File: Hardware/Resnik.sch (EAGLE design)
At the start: 194 parts, among them IC1 ATMEGA644M, J1 CONN_82.54_SCREW, J3 CONN_42.54_SCREW, J4 CONN_82.54_SCREW, Q1 DMG3404, Q2 DMG3404, Q3 FDN360P, Q4 FDN360P, Q5 FDN360P, Q6 DMG3404, U1 TLV61220DBV, U10 TPS22917DBV, U11 SN74AUP1G04YFP, U12 SN74AUP1G04YFP, U13 SN74AUP2G86SOT833-1, U14 SN74AUP2G08DQE, U15 SN74AUP2G08DQE, U16 SN74AUP2G08DQE, U17 MIC2544MSOP, U18 MIC2544MSOP, U19 MIC2544MSOP, U2 TPS62822DLC, U20 MIC2544MSOP, U21 TPS22917DBV, U22 TPS22917DBV, U23 FT231X-Q, U24 SN74LVC1G3157DRL, U25 SN74AUP3G34DCU, U26 TXS0102DQM, U27 TXS0108RGY, U28 TXS0108RGY, U29 TXS0104RGY, U3 TPS61032RSA, U30 MCP4726A2SOT-23, U31 BME280, U32 ADS1115, U33 ADS1115, U34 INA211DCK, U35 INA210DCK, U36 TCA9535RTW, U37 TLV3691DCK, U38 TS5A21366RSE, U39 MIC94090C6, U5 BQ2980RUG, U6 TPS2105, U7 LTC4412S6, U8 TPL5111DDC, U9 TPS79733

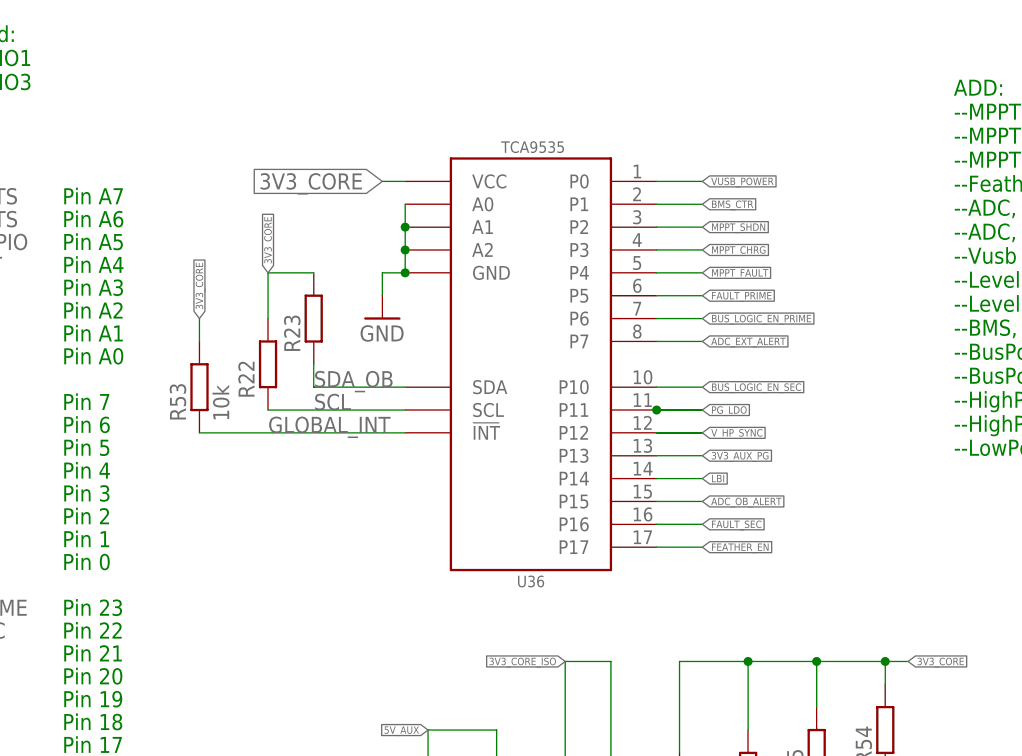
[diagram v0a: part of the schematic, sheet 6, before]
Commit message: Initial updates for v0.3
Additional routing required, need to add ADC switch enable, need to add efficiency modification to mppt
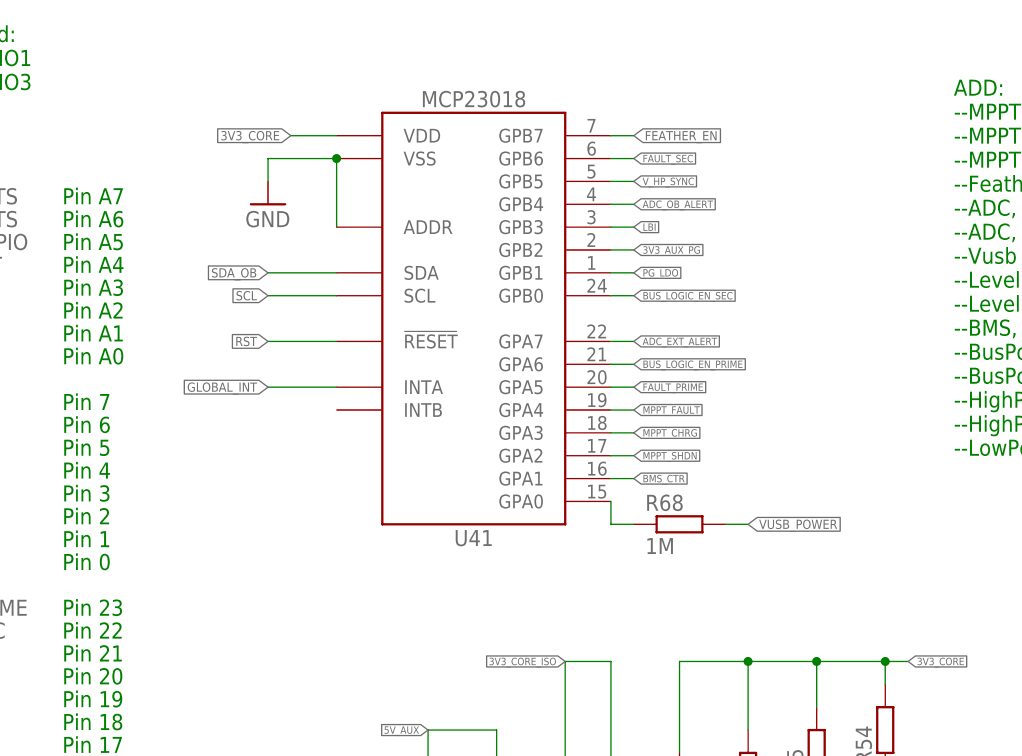
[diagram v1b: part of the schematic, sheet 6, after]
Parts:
- removed R22: (no value), bschulz_passives:R-EU_R0402
- removed U36: TCA9535RTW, bschulz:TCA9535RTW
- added Q7: 2N7002, bschulz:MOSFET-NCH-2N7002PW
- added R63: 100k, bschulz_passives:R-EU_100KR0402
- added R64, R68: 1M, bschulz_passives:R-EU_1MR0402
- added R65, R66: 180k, bschulz_passives:R-EU_180KR0402
- added R67: 10k, bschulz_passives:R-EU_10KR0402
- added U40: SN74AHC1G86DCK, bschulz:SN74AHC1G86DCK
- added U41: MCP23018QFN, bschulz:MCP23018QFN
- R23: value (none) -> 100k; device bschulz_passives:R-EU_R0402 -> bschulz_passives:R-EU_100KR0402
- R53: value 10k -> 1M; device bschulz_passives:R-EU_10KR0402 -> bschulz_passives:R-EU_1MR0402
- U13: value SN74AUP2G86SOT833-1 -> SN74AUP1G04YFP; device bschulz:SN74AUP2G86SOT833-1 -> bschulz:SN74AUP1G04YFP
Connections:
- removed net N$22: U13.Y1, U16.A1
- removed net N$25: U13.Y2, U16.A2
- new net N$17: R68.1, U41.GPA0
- new net N$68: Q7.G, U13.Y
- new net POWER_EN: U13.A, U16.A1, U16.A2, U2.EN, U3.EN, U40.Y
- new net VCC: U40.VCC
- net 3V3_AUX_PG: now also U41.GPB2; no longer U36.P13
- net 3V3_CORE: now also U41.VDD; no longer R22.2, R23.2, R53.2, U36.VCC
- net 3V3_CORE_ISO: now also R23.2
- net 5V_AUX: now also Q7.D, R67.2; no longer U2.EN
- net ADC_EXT_ALERT: now also U41.GPA7; no longer U36.P7
- net ADC_OB_ALERT: now also U41.GPB4; no longer U36.P15
- net BMS_CTR: now also U41.GPA1; no longer U36.P1
- net BUS_LOGIC_EN_PRIME: now also U41.GPA6; no longer U36.P6
- net BUS_LOGIC_EN_SEC: now also U41.GPB0; no longer U36.P10
- net C0: now also U40.A, U40.B; no longer U13.A1, U13.B2
- net C1: no longer U13.A2, U13.B1
- net FAULT_PRIME: now also U41.GPA5; no longer U36.P5
- net FAULT_SEC: now also U41.GPB6; no longer U36.P16
- net FEATHER_EN: now also U41.GPB7; no longer U36.P17
- net GLOBAL_INT: now also U41.INTA; no longer R53.1, U36.!INT
- net GND: now also Q7.S, R23.1, R53.1, R63.1, R64.1, R65.1, R66.1, R67.1, U40.GND, U41.ADDR, U41.VSS; no longer U36.A0, U36.A1, U36.A2, U36.GND
- net LBI: now also U41.GPB3; no longer U36.P14
- net MPPT_CHRG: now also U41.GPA3; no longer U36.P3
- net MPPT_FAULT: now also U41.GPA4; no longer U36.P4
- net MPPT_SHDN: now also U41.GPA2; no longer U36.P2
- net PG_LDO: now also U41.GPB1; no longer U36.P11
- net RST: now also U41.!RESET
- net SCL: now also U41.SCL; no longer R22.1, U36.SCL
- net SDA_OB: now also U41.SDA; no longer R23.1, U36.SDA
- net VBUS_PRIME: now also R65.2
- net VBUS_SEC: now also R66.2
- net VUSB_POWER: now also R63.2, R68.2; no longer U36.P0
- net V_HP: no longer U3.EN
- net V_HP_SYNC: now also U41.GPB5; no longer U36.P12
- net V_LI_SENSE: now also R64.2
- net V_PRIME_SENSE: now also R53.2
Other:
- moved on the sheet: C1, R1, R2, R3, R8

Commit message: Layout updates, cleanup required, minor testing
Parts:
- removed R54: (no value), bschulz_passives:R-EU_R0402
- added Q8: 2N7002, bschulz:MOSFET-NCH-2N7002PW
- added R22, R69, R70, R71: (no value), bschulz_passives:R-EU_R0603
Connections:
- removed net N$67: C10.1, D1.C, U4.VIN, U4.VIN_REG
- removed net VCC: U40.VCC
- new net ADC_SENSE_SW: IC1.(PCINT8/XCK0/T0)PB0, U38.S1, U38.S2
- new net MPPT_VIN_REG: R22.1, R69.2, U4.VIN_REG
- new net N$22: Q8.D, R70.1
- new net V_SOLAR_IN: C10.1, D1.C, R22.2, R71.2, U4.VIN
- net 3V3_CORE: now also U40.VCC; no longer R54.2
- net 5V_AUX: no longer U38.S1, U38.S2
- net C0: no longer U40.B
- net C1: now also U40.B
- net GND: now also Q8.S, R69.1
- net MPPT_CHRG: now also Q8.G
- net MPPT_SHDN: now also R70.2, R71.1; no longer R54.1, U41.GPA2

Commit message: Continued layout, generated gerbers
Improved layout, generated gerbers, final design review before send to fab
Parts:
- added D8: BAT54C, bschulz:BAT54C
- R18: value 5m -> 50m; device bschulz_passives:R-EU_0.005R0805 -> bschulz_passives:R-EU_0.05R0805
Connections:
- new net N$69: D8.C, U37.VCC
- net 5V_LP: now also D8.A2
- net V_CORE: no longer U37.VCC
- net V_PRIME: now also D8.A1
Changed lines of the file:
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@@
 <setting verticaltext="up"/>
 </settings>
-<grid distance="0.1" unitdist="inch" unit="mm" style="lines" multiple="1" display="no" altdistance="0.01" altunitdist="inch" altunit="mm"/>
+<grid distance="0.1" unitdist="inch" unit="inch" style="lines" multiple="1" display="no" altdistance="0.01" altunitdist="inch" altunit="inch"/>
 <layers>
 <layer number="1" name="Top" color="4" fill="1" visible="no" active="no"/>
@@
 <attribute name="MPN" value="CMDSH2-3 TR"/>
 </part>
-<part name="R18" library="bschulz_passives" deviceset="R-EU_" device="R0805" technology="0.005" value="5m"/>
+<part name="R18" library="bschulz_passives" deviceset="R-EU_" device="R0805" technology="0.05" value="50m"/>
 <part name="L4" library="bschulz" deviceset="INDUCTOR" device="MAIA_4.1X4.1" value="4.7uH">
 <attribute name="DIGIKEY" value="732-11316-1-ND"/>
@@
 <part name="R71" library="bschulz_passives" deviceset="R-EU_" device="R0603"/>
 <part name="GND85" library="supply1" library_urn="urn:adsk.eagle:library:371" deviceset="GND" device=""/>
+<part name="D8" library="bschulz" deviceset="BAT54C" device=""/>
 </parts>
 <sheets>
@@
 <attribute name="VALUE" x="175.26" y="-10.16" size="1.778" layer="96"/>
 </instance>
+<instance part="D8" gate="G$1" x="251.46" y="165.1" smashed="yes" rot="R270">
+<attribute name="NAME" x="253.4666" y="164.338" size="1.778" layer="95" rot="R270"/>
+<attribute name="VALUE" x="247.4976" y="169.418" size="1.778" layer="96" rot="R270"/>
+</instance>
 </instances>
 <busses>
@@
 <wire x1="264.16" y1="160.02" x2="259.08" y2="160.02" width="0.1524" layer="91"/>
 <label x="256.54" y="160.02" size="1.27" layer="95"/>
+</segment>
+<segment>
+<pinref part="D8" gate="G$1" pin="A2"/>
+<wire x1="251.46" y1="160.02" x2="251.46" y2="157.48" width="0.1524" layer="91"/>
+<wire x1="251.46" y1="157.48" x2="248.92" y2="157.48" width="0.1524" layer="91"/>
+<label x="248.92" y="157.48" size="1.778" layer="95" rot="R180" xref="yes"/>
 </segment>
 </net>
@@
 <label x="256.54" y="157.48" size="1.27" layer="95"/>
 </segment>
+<segment>
+<pinref part="D8" gate="G$1" pin="A1"/>
+<wire x1="251.46" y1="170.18" x2="251.46" y2="172.72" width="0.1524" layer="91"/>
+<wire x1="251.46" y1="172.72" x2="248.92" y2="172.72" width="0.1524" layer="91"/>
+<label x="248.92" y="172.72" size="1.778" layer="95" rot="R180" xref="yes"/>
+</segment>
 </net>
 <net name="3V3_CORE" class="0">
@@
 <wire x1="307.34" y1="139.7" x2="325.12" y2="139.7" width="0.1524" layer="91"/>
 <junction x="307.34" y="139.7"/>
-</segment>
-<segment>
-<pinref part="U37" gate="G$1" pin="VCC"/>
-<wire x1="264.16" y1="165.1" x2="259.08" y2="165.1" width="0.1524" layer="91"/>
-<label x="256.54" y="165.1" size="1.27" layer="95"/>
 </segment>
 </net>
@@
 </segment>
 </net>
+<net name="N$69" class="0">
+<segment>
+<pinref part="D8" gate="G$1" pin="C"/>
+<pinref part="U37" gate="G$1" pin="VCC"/>
+<wire x1="254" y1="165.1" x2="264.16" y2="165.1" width="0.1524" layer="91"/>
+</segment>
+</net>

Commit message: Naming/part cleanup
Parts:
- R12: value (none) -> 1k
- R22: value (none) -> 143k
- R51: value (none) -> 20k; device bschulz:R-EU_R0603 -> bschulz_passives:R-EU_R0603
- R55, R56, R59, R71: value (none) -> 1M
- R57, R58, R60, R61, R69: value (none) -> 100k
- R70: value (none) -> 200k
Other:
- note added: "Pin A0/24"
- note added: "Pin A1/25"
- note added: "Pin A2/26"
- note added: "Pin A3/27"
- note added: "Pin A4/28"
- note added: "Pin A5/29"
- note added: "Pin A6/30"
- note added: "Pin A7/31"
- note removed: "Pin A0"
- note removed: "Pin A1"
- note removed: "Pin A2"
- note removed: "Pin A3"
- note removed: "Pin A4"
- note removed: "Pin A5"
- note removed: "Pin A6"
- note removed: "Pin A7"
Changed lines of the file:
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@@
 <?xml version="1.0" encoding="utf-8"?>
 <!DOCTYPE eagle SYSTEM "eagle.dtd">
-<eagle version="9.2.1">
+<eagle version="9.4.2">
 <drawing>
 <settings>
@@
 <part name="R11" library="bschulz_passives" deviceset="R-EU_" device="R0402" technology="20" value="20"/>
 <part name="R9" library="bschulz_passives" deviceset="R-EU_" device="R0402" technology="330" value="330"/>
-<part name="R12" library="bschulz_passives" deviceset="R-EU_" device="R0402"/>
+<part name="R12" library="bschulz_passives" deviceset="R-EU_" device="R0402" value="1k"/>
 <part name="R14" library="bschulz_passives" deviceset="R-EU_" device="R0402" technology="100" value="100R"/>
 <part name="R15" library="bschulz_passives" deviceset="R-EU_" device="R0402" technology="2K" value="2k"/>
@@
 <part name="U34" library="bschulz" deviceset="INA21*" device="DCK" technology="1"/>
 <part name="D7" library="bschulz" deviceset="LM4040" device="" technology="2.5"/>
-<part name="R51" library="bschulz" deviceset="R-EU_" device="R0603"/>
+<part name="R51" library="bschulz_passives" deviceset="R-EU_" device="R0603" value="20k"/>
 <part name="GND64" library="supply1" library_urn="urn:adsk.eagle:library:371" deviceset="GND" device=""/>
 <part name="C37" library="bschulz_passives" deviceset="C-EU" device="C0402" technology="0.1UF" value="0.1uF"/>
@@
 <part name="GND52" library="supply1" library_urn="urn:adsk.eagle:library:371" deviceset="GND" device=""/>
 <part name="H3" library="bschulz" deviceset="MOUNTING_HOLE" device="4_NP"/>
-<part name="R55" library="bschulz_passives" deviceset="R-EU_" device="R0402"/>
-<part name="R56" library="bschulz_passives" deviceset="R-EU_" device="R0402"/>
-<part name="R57" library="bschulz_passives" deviceset="R-EU_" device="R0402"/>
-<part name="R58" library="bschulz_passives" deviceset="R-EU_" device="R0402"/>
-<part name="R59" library="bschulz_passives" deviceset="R-EU_" device="R0402"/>
-<part name="R60" library="bschulz_passives" deviceset="R-EU_" device="R0402"/>
-<part name="R61" library="bschulz_passives" deviceset="R-EU_" device="R0402"/>
+<part name="R55" library="bschulz_passives" deviceset="R-EU_" device="R0402" value="1M"/>
+<part name="R56" library="bschulz_passives" deviceset="R-EU_" device="R0402" value="1M"/>
+<part name="R57" library="bschulz_passives" deviceset="R-EU_" device="R0402" value="100k"/>
+<part name="R58" library="bschulz_passives" deviceset="R-EU_" device="R0402" value="100k"/>
+<part name="R59" library="bschulz_passives" deviceset="R-EU_" device="R0402" value="1M"/>
+<part name="R60" library="bschulz_passives" deviceset="R-EU_" device="R0402" value="100k"/>
+<part name="R61" library="bschulz_passives" deviceset="R-EU_" device="R0402" value="100k"/>
 <part name="GND31" library="supply1" library_urn="urn:adsk.eagle:library:371" deviceset="GND" device=""/>
 <part name="GND30" library="supply1" library_urn="urn:adsk.eagle:library:371" deviceset="GND" device=""/>
@@
 <part name="GND84" library="supply1" library_urn="urn:adsk.eagle:library:371" deviceset="GND" device=""/>
 <part name="R68" library="bschulz_passives" deviceset="R-EU_" device="R0402" technology="1M" value="1M"/>
-<part name="R22" library="bschulz_passives" deviceset="R-EU_" device="R0603"/>
-<part name="R69" library="bschulz_passives" deviceset="R-EU_" device="R0603"/>
+<part name="R22" library="bschulz_passives" deviceset="R-EU_" device="R0603" value="143k"/>
+<part name="R69" library="bschulz_passives" deviceset="R-EU_" device="R0603" value="100k"/>
 <part name="GND70" library="supply1" library_urn="urn:adsk.eagle:library:371" deviceset="GND" device=""/>
 <part name="Q8" library="bschulz" deviceset="MOSFET-NCH" device="-2N7002PW" value="2N7002"/>
-<part name="R70" library="bschulz_passives" deviceset="R-EU_" device="R0603"/>
-<part name="R71" library="bschulz_passives" deviceset="R-EU_" device="R0603"/>
+<part name="R70" library="bschulz_passives" deviceset="R-EU_" device="R0603" value="200k"/>
+<part name="R71" library="bschulz_passives" deviceset="R-EU_" device="R0603" value="1M"/>
 <part name="GND85" library="supply1" library_urn="urn:adsk.eagle:library:371" deviceset="GND" device=""/>
 <part name="D8" library="bschulz" deviceset="BAT54C" device=""/>
@@
 <plain>
 <text x="116.84" y="27.94" size="1.778" layer="91">Pin 12</text>
-<text x="116.84" y="104.14" size="1.778" layer="91">Pin A7</text>
-<text x="116.84" y="101.6" size="1.778" layer="91">Pin A6</text>
-<text x="116.84" y="99.06" size="1.778" layer="91">Pin A5</text>
-<text x="116.84" y="96.52" size="1.778" layer="91">Pin A4</text>
+<text x="116.84" y="104.14" size="1.778" layer="91">Pin A7/31</text>
+<text x="116.84" y="101.6" size="1.778" layer="91">Pin A6/30</text>
+<text x="116.84" y="99.06" size="1.778" layer="91">Pin A5/29</text>
+<text x="116.84" y="96.52" size="1.778" layer="91">Pin A4/28</text>
 <text x="116.84" y="35.56" size="1.778" layer="91">Pin 15</text>
 <text x="116.84" y="58.42" size="1.778" layer="91">Pin 23</text>
-<text x="116.84" y="93.98" size="1.778" layer="91">Pin A3</text>
+<text x="116.84" y="93.98" size="1.778" layer="91">Pin A3/27</text>
 <text x="124.46" y="27.94" size="1.778" layer="91">Also ext PWM</text>
 <text x="116.84" y="48.26" size="1.778" layer="91">Pin 19</text>
@@
 <text x="116.84" y="66.04" size="1.778" layer="91">Pin 1</text>
 <text x="116.84" y="73.66" size="1.778" layer="91">Pin 4</text>
-<text x="116.84" y="86.36" size="1.778" layer="91">Pin A0</text>
-<text x="116.84" y="88.9" size="1.778" layer="91">Pin A1</text>
-<text x="116.84" y="91.44" size="1.778" layer="91">Pin A2</text>
+<text x="116.84" y="86.36" size="1.778" layer="91">Pin A0/24</text>
+<text x="116.84" y="88.9" size="1.778" layer="91">Pin A1/25</text>
+<text x="116.84" y="91.44" size="1.778" layer="91">Pin A2/26</text>
 <text x="116.84" y="50.8" size="1.778" layer="91">Pin 20</text>
 <text x="116.84" y="25.4" size="1.778" layer="91">Pin 11</text>
